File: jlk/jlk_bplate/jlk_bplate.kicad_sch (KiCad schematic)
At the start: 16 parts

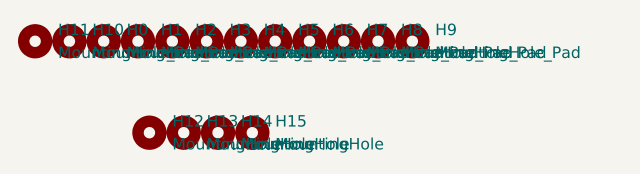
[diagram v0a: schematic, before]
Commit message: Switched to SMD diode, col2row.
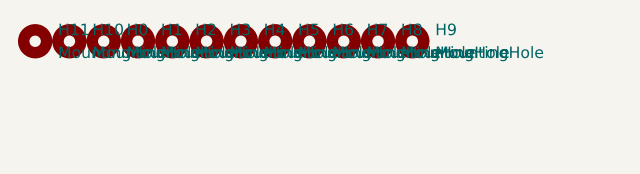
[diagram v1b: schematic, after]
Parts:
- removed H12, H13, H14, H15: MountingHole, MountingHole:MountingHole_2.2mm_M2_ISO7380_Pad, symbol Mechanical:MountingHole
- H0, H1, H10, H11, H2, H3, H4, H5, H6, H7, H8, H9: value MountingHole_Pad -> MountingHole
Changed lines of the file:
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@@
       (effects (font (size 1.27 1.27)) (justify left))
     )
-    (property "Value" "MountingHole_Pad" (at 363.22 34.29 0)
+    (property "Value" "MountingHole" (at 363.22 34.29 0)
       (effects (font (size 1.27 1.27)) (justify left))
     )
@@
       (effects (font (size 1.27 1.27)) (justify left))
     )
-    (property "Value" "MountingHole_Pad" (at 389.89 34.29 0)
+    (property "Value" "MountingHole" (at 389.89 34.29 0)
       (effects (font (size 1.27 1.27)) (justify left))
     )
@@
     )
   )
-  (symbol (lib_id "Mechanical:MountingHole") (at 373.38 43.18 0) (unit 1)
-    (in_bom yes) (on_board yes) (dnp no) (fields_autoplaced)
-    (property "Reference" "H15" (at 375.92 41.91 0)
-      (effects (font (size 1.27 1.27)) (justify left))
-    )
-    (property "Value" "MountingHole" (at 375.92 44.45 0)
-      (effects (font (size 1.27 1.27)) (justify left))
-    )
-    (property "Footprint" "MountingHole:MountingHole_2.2mm_M2_ISO7380_Pad" (at 373.38 43.18 0)
-      (effects (font (size 1.27 1.27)) hide)
-    )
-    (property "Datasheet" "~" (at 373.38 43.18 0)
-      (effects (font (size 1.27 1.27)) hide)
-    )
-    (instances
-      (project "jlk_bplate"
-        (path "/97127b28-60f4-45ff-835e-dccfbc833331"
-          (reference "H15") (unit 1)
-        )
-      )
-    )
-  )
   (symbol (lib_id "Mechanical:MountingHole") (at 391.16 33.02 0) (unit 1)
     (in_bom yes) (on_board yes) (dnp no) (fields_autoplaced)
@@
       (effects (font (size 1.27 1.27)) (justify left))
     )
-    (property "Value" "MountingHole_Pad" (at 393.7 34.29 0)
+    (property "Value" "MountingHole" (at 393.7 34.29 0)
       (effects (font (size 1.27 1.27)) (justify left))
     )
@@
       (effects (font (size 1.27 1.27)) (justify left))
     )
-    (property "Value" "MountingHole_Pad" (at 382.27 34.29 0)
+    (property "Value" "MountingHole" (at 382.27 34.29 0)
       (effects (font (size 1.27 1.27)) (justify left))
     )
@@
       (effects (font (size 1.27 1.27)) (justify left))
     )
-    (property "Value" "MountingHole_Pad" (at 367.03 34.29 0)
+    (property "Value" "MountingHole" (at 367.03 34.29 0)
       (effects (font (size 1.27 1.27)) (justify left))
     )
@@
       (effects (font (size 1.27 1.27)) (justify left))
     )
-    (property "Value" "MountingHole_Pad" (at 374.65 34.29 0)
+    (property "Value" "MountingHole" (at 374.65 34.29 0)
       (effects (font (size 1.27 1.27)) (justify left))
     )
@@
     )
   )
-  (symbol (lib_id "Mechanical:MountingHole") (at 369.57 43.18 0) (unit 1)
-    (in_bom yes) (on_board yes) (dnp no) (fields_autoplaced)
-    (property "Reference" "H14" (at 372.11 41.91 0)
-      (effects (font (size 1.27 1.27)) (justify left))
-    )
-    (property "Value" "MountingHole" (at 372.11 44.45 0)
-      (effects (font (size 1.27 1.27)) (justify left))
-    )
-    (property "Footprint" "MountingHole:MountingHole_2.2mm_M2_ISO7380_Pad" (at 369.57 43.18 0)
-      (effects (font (size 1.27 1.27)) hide)
-    )
-    (property "Datasheet" "~" (at 369.57 43.18 0)
-      (effects (font (size 1.27 1.27)) hide)
-    )
-    (instances
-      (project "jlk_bplate"
-        (path "/97127b28-60f4-45ff-835e-dccfbc833331"
-          (reference "H14") (unit 1)
-        )
-      )
-    )
-  )
   (symbol (lib_id "Mechanical:MountingHole") (at 368.3 33.02 0) (unit 1)
     (in_bom yes) (on_board yes) (dnp no) (fields_autoplaced)
@@
       (effects (font (size 1.27 1.27)) (justify left))
     )
-    (property "Value" "MountingHole_Pad" (at 370.84 34.29 0)
+    (property "Value" "MountingHole" (at 370.84 34.29 0)
       (effects (font (size 1.27 1.27)) (justify left))
     )
@@
     )
   )
-  (symbol (lib_id "Mechanical:MountingHole") (at 361.95 43.18 0) (unit 1)
-    (in_bom yes) (on_board yes) (dnp no) (fields_autoplaced)
-    (property "Reference" "H12" (at 364.49 41.91 0)
-      (effects (font (size 1.27 1.27)) (justify left))
-    )
-    (property "Value" "MountingHole" (at 364.49 44.45 0)
-      (effects (font (size 1.27 1.27)) (justify left))
-    )
-    (property "Footprint" "MountingHole:MountingHole_2.2mm_M2_ISO7380_Pad" (at 361.95 43.18 0)
-      (effects (font (size 1.27 1.27)) hide)
-    )
-    (property "Datasheet" "~" (at 361.95 43.18 0)
-      (effects (font (size 1.27 1.27)) hide)
-    )
-    (instances
-      (project "jlk_bplate"
-        (path "/97127b28-60f4-45ff-835e-dccfbc833331"
-          (reference "H12") (unit 1)
-        )
-      )
-    )
-  )
   (symbol (lib_id "Mechanical:MountingHole") (at 375.92 33.02 0) (unit 1)
     (in_bom yes) (on_board yes) (dnp no) (fields_autoplaced)
@@
       (effects (font (size 1.27 1.27)) (justify left))
     )
-    (property "Value" "MountingHole_Pad" (at 378.46 34.29 0)
+    (property "Value" "MountingHole" (at 378.46 34.29 0)
       (effects (font (size 1.27 1.27)) (justify left))
     )
@@
       (effects (font (size 1.27 1.27)) (justify left))
     )
-    (property "Value" "MountingHole_Pad" (at 351.79 34.29 0)
+    (property "Value" "MountingHole" (at 351.79 34.29 0)
       (effects (font (size 1.27 1.27)) (justify left))
     )
@@
       (effects (font (size 1.27 1.27)) (justify left))
     )
-    (property "Value" "MountingHole_Pad" (at 386.08 34.29 0)
+    (property "Value" "MountingHole" (at 386.08 34.29 0)
       (effects (font (size 1.27 1.27)) (justify left))
     )
@@
       (effects (font (size 1.27 1.27)) (justify left))
     )
-    (property "Value" "MountingHole_Pad" (at 355.6 34.29 0)
+    (property "Value" "MountingHole" (at 355.6 34.29 0)
       (effects (font (size 1.27 1.27)) (justify left))
     )
@@
       (effects (font (size 1.27 1.27)) (justify left))
     )
-    (property "Value" "MountingHole_Pad" (at 359.41 34.29 0)
+    (property "Value" "MountingHole" (at 359.41 34.29 0)
       (effects (font (size 1.27 1.27)) (justify left))
     )
@@
         )
       )
-    )
-  )
-  (symbol (lib_id "Mechanical:MountingHole") (at 365.76 43.18 0) (unit 1)
-    (in_bom yes) (on_board yes) (dnp no) (fields_autoplaced)
-    (property "Reference" "H13" (at 368.3 41.91 0)
-      (effects (font (size 1.27 1.27)) (justify left))
-    )
-    (property "Value" "MountingHole" (at 368.3 44.45 0)
-      (effects (font (size 1.27 1.27)) (justify left))
-    )
-    (property "Footprint" "MountingHole:MountingHole_2.2mm_M2_ISO7380_Pad" (at 365.76 43.18 0)
-      (effects (font (size 1.27 1.27)) hide)
-    )
-    (property "Datasheet" "~" (at 365.76 43.18 0)
-      (effects (font (size 1.27 1.27)) hide)
-    )
-    (instances
-      (project "jlk_bplate"
-        (path "/97127b28-60f4-45ff-835e-dccfbc833331"
-          (reference "H13") (unit 1)
-        )
-      )

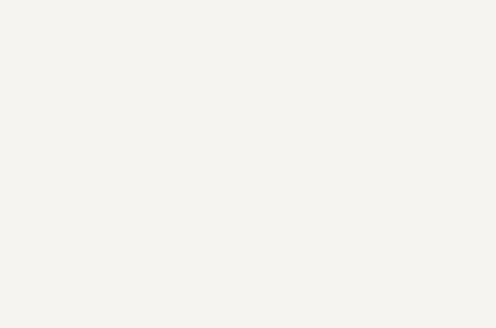
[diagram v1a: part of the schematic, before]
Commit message: Changed the reset button on the jlk.
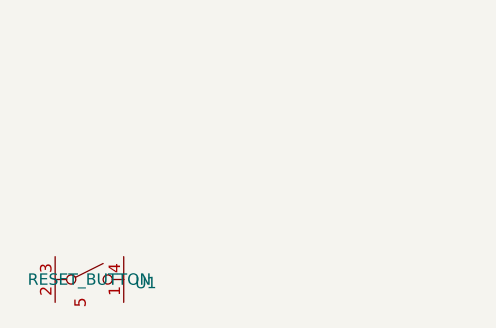
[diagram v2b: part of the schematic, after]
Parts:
- added U1: RESET_BUTTON, MountingHole:MountingHole_8.4mm_M8, symbol symbols:RESET_BUTTON
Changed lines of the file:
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@@
+    )
+  )
+  (symbol (lib_id "symbols:RESET_BUTTON") (at 212.09 152.4 270) (unit 1)
+    (in_bom yes) (on_board yes) (dnp no) (fields_autoplaced)
+    (property "Reference" "U1" (at 217.17 152.781 90)
+      (effects (font (size 1.27 1.27)) (justify left))
+    )
+    (property "Value" "RESET_BUTTON" (at 212.09 152.4 90)
+      (effects (font (size 1.27 1.27)))
+    )
+    (property "Footprint" "MountingHole:MountingHole_8.4mm_M8" (at 212.09 152.4 90)
+      (effects (font (size 1.27 1.27)) hide)
+    )
+    (property "Datasheet" "" (at 212.09 152.4 90)
+      (effects (font (size 1.27 1.27)) hide)
+    )
+    (pin "2")
+    (pin "3")
+    (pin "4")
+    (pin "5")
+    (pin "1")
+    (instances
+      (project "jlk_bplate"
+        (path "/97127b28-60f4-45ff-835e-dccfbc833331"
+          (reference "U1") (unit 1)
+        )
+      )
     )
   )

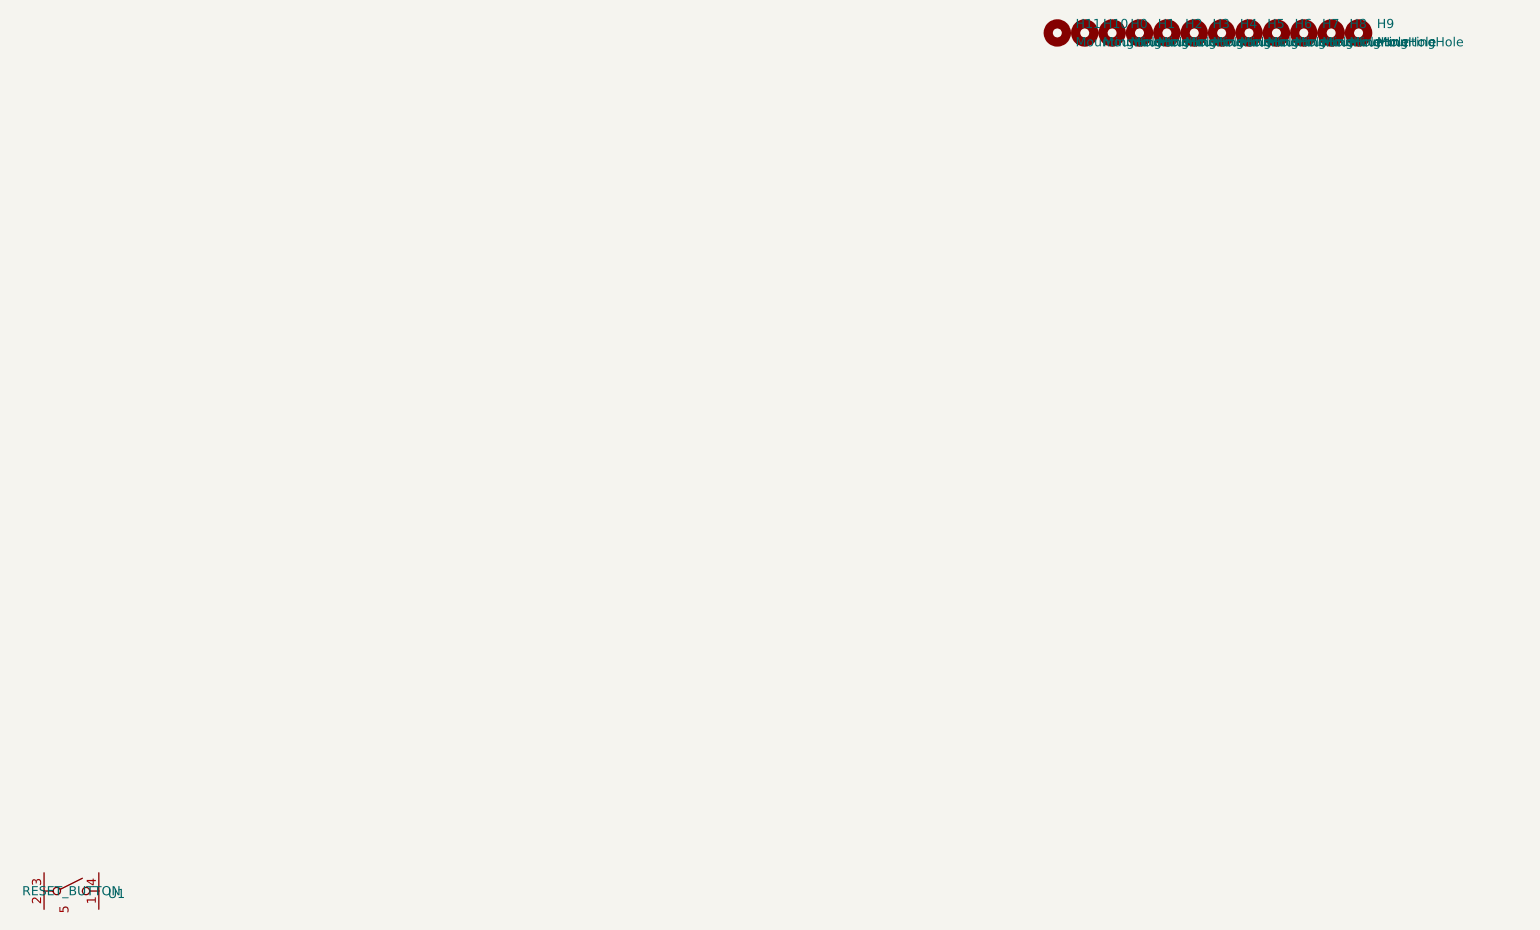
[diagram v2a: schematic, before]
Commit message: Changed jlk for mounting promicro under the pcb.
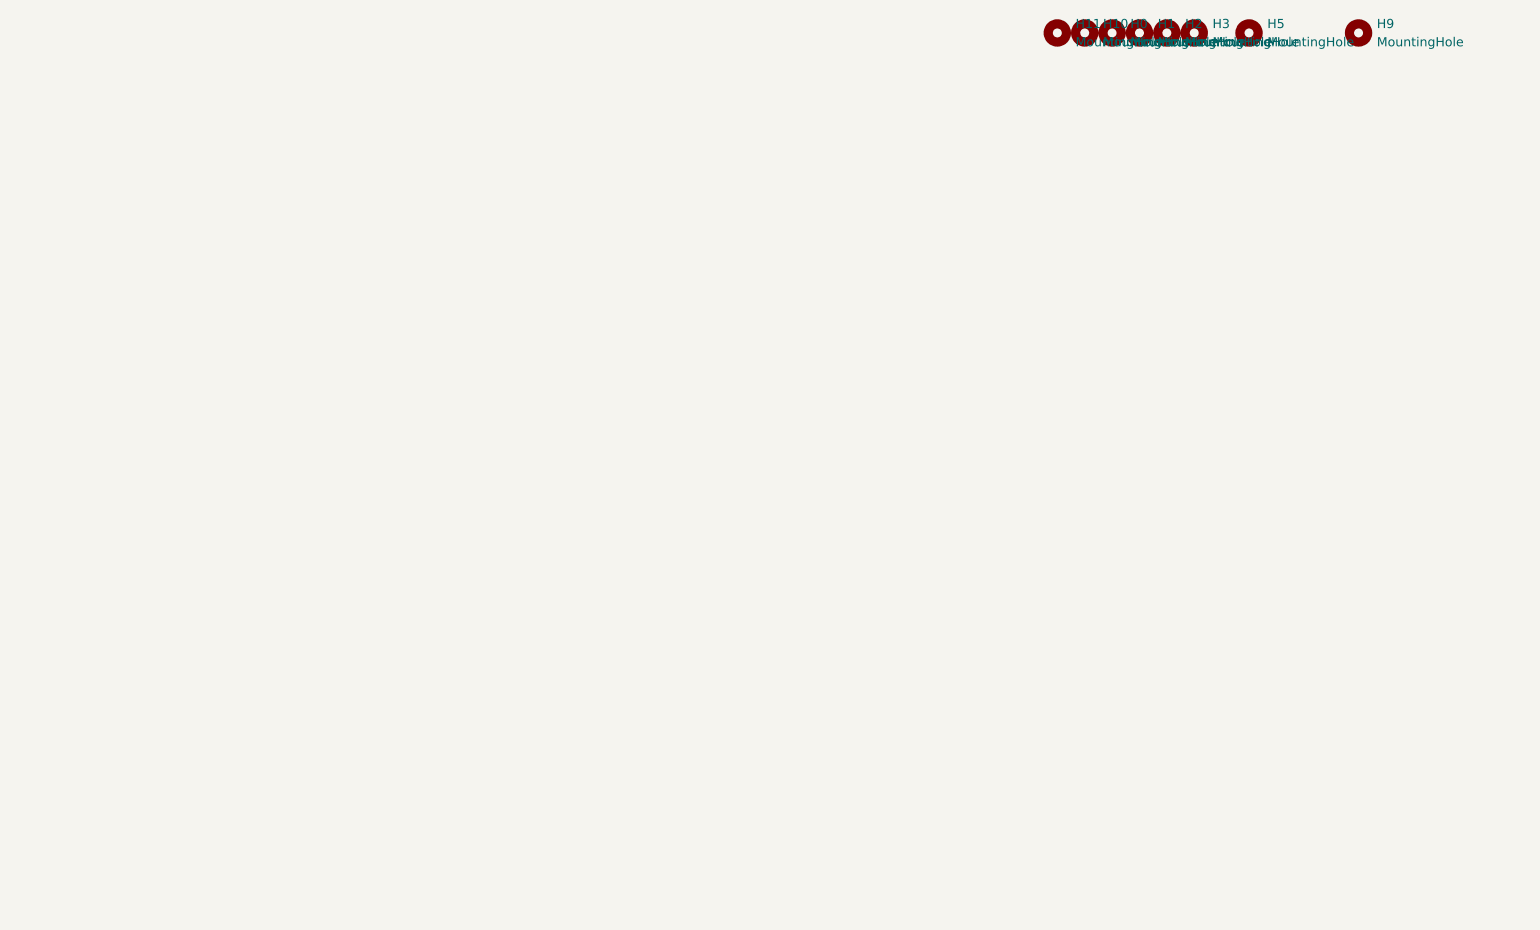
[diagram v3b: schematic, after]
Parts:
- removed H4, H6, H7, H8: MountingHole, MountingHole:MountingHole_2.2mm_M2_ISO7380_Pad, symbol Mechanical:MountingHole
- removed U1: RESET_BUTTON, MountingHole:MountingHole_8.4mm_M8, symbol symbols:RESET_BUTTON
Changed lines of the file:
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@@
-    )
-  )
-  (symbol (lib_id "Mechanical:MountingHole") (at 387.35 33.02 0) (unit 1)
-    (in_bom yes) (on_board yes) (dnp no) (fields_autoplaced)
-    (property "Reference" "H8" (at 389.89 31.75 0)
-      (effects (font (size 1.27 1.27)) (justify left))
-    )
-    (property "Value" "MountingHole" (at 389.89 34.29 0)
-      (effects (font (size 1.27 1.27)) (justify left))
-    )
-    (property "Footprint" "MountingHole:MountingHole_2.2mm_M2_ISO7380_Pad" (at 387.35 33.02 0)
-      (effects (font (size 1.27 1.27)) hide)
-    )
-    (property "Datasheet" "~" (at 387.35 33.02 0)
-      (effects (font (size 1.27 1.27)) hide)
-    )
-    (instances
-      (project "jlk_bplate"
-        (path "/97127b28-60f4-45ff-835e-dccfbc833331"
-          (reference "H8") (unit 1)
-        )
-      )
     )
   )
@@
     )
   )
-  (symbol (lib_id "symbols:RESET_BUTTON") (at 212.09 152.4 270) (unit 1)
-    (in_bom yes) (on_board yes) (dnp no) (fields_autoplaced)
-    (property "Reference" "U1" (at 217.17 152.781 90)
-      (effects (font (size 1.27 1.27)) (justify left))
-    )
-    (property "Value" "RESET_BUTTON" (at 212.09 152.4 90)
-      (effects (font (size 1.27 1.27)))
-    )
-    (property "Footprint" "MountingHole:MountingHole_8.4mm_M8" (at 212.09 152.4 90)
-      (effects (font (size 1.27 1.27)) hide)
-    )
-    (property "Datasheet" "" (at 212.09 152.4 90)
-      (effects (font (size 1.27 1.27)) hide)
-    )
-    (pin "2")
-    (pin "3")
-    (pin "4")
-    (pin "5")
-    (pin "1")
-    (instances
-      (project "jlk_bplate"
-        (path "/97127b28-60f4-45ff-835e-dccfbc833331"
-          (reference "U1") (unit 1)
-        )
-      )
-    )
-  )
-  (symbol (lib_id "Mechanical:MountingHole") (at 379.73 33.02 0) (unit 1)
-    (in_bom yes) (on_board yes) (dnp no) (fields_autoplaced)
-    (property "Reference" "H6" (at 382.27 31.75 0)
-      (effects (font (size 1.27 1.27)) (justify left))
-    )
-    (property "Value" "MountingHole" (at 382.27 34.29 0)
-      (effects (font (size 1.27 1.27)) (justify left))
-    )
-    (property "Footprint" "MountingHole:MountingHole_2.2mm_M2_ISO7380_Pad" (at 379.73 33.02 0)
-      (effects (font (size 1.27 1.27)) hide)
-    )
-    (property "Datasheet" "~" (at 379.73 33.02 0)
-      (effects (font (size 1.27 1.27)) hide)
-    )
-    (instances
-      (project "jlk_bplate"
-        (path "/97127b28-60f4-45ff-835e-dccfbc833331"
-          (reference "H6") (unit 1)
-        )
-      )
-    )
-  )
   (symbol (lib_id "Mechanical:MountingHole") (at 364.49 33.02 0) (unit 1)
     (in_bom yes) (on_board yes) (dnp no) (fields_autoplaced)
@@
         (path "/97127b28-60f4-45ff-835e-dccfbc833331"
           (reference "H2") (unit 1)
-        )
-      )
-    )
-  )
-  (symbol (lib_id "Mechanical:MountingHole") (at 372.11 33.02 0) (unit 1)
-    (in_bom yes) (on_board yes) (dnp no) (fields_autoplaced)
-    (property "Reference" "H4" (at 374.65 31.75 0)
-      (effects (font (size 1.27 1.27)) (justify left))
-    )
-    (property "Value" "MountingHole" (at 374.65 34.29 0)
-      (effects (font (size 1.27 1.27)) (justify left))
-    )
-    (property "Footprint" "MountingHole:MountingHole_2.2mm_M2_ISO7380_Pad" (at 372.11 33.02 0)
-      (effects (font (size 1.27 1.27)) hide)
-    )
-    (property "Datasheet" "~" (at 372.11 33.02 0)
-      (effects (font (size 1.27 1.27)) hide)
-    )
-    (instances
-      (project "jlk_bplate"
-        (path "/97127b28-60f4-45ff-835e-dccfbc833331"
-          (reference "H4") (unit 1)
         )
       )
@@
         )
       )
-    )
-  )
-  (symbol (lib_id "Mechanical:MountingHole") (at 383.54 33.02 0) (unit 1)
-    (in_bom yes) (on_board yes) (dnp no) (fields_autoplaced)
-    (property "Reference" "H7" (at 386.08 31.75 0)
-      (effects (font (size 1.27 1.27)) (justify left))
-    )
-    (property "Value" "MountingHole" (at 386.08 34.29 0)
-      (effects (font (size 1.27 1.27)) (justify left))
-    )
-    (property "Footprint" "MountingHole:MountingHole_2.2mm_M2_ISO7380_Pad" (at 383.54 33.02 0)
-      (effects (font (size 1.27 1.27)) hide)
-    )
-    (property "Datasheet" "~" (at 383.54 33.02 0)
-      (effects (font (size 1.27 1.27)) hide)
-    )
-    (instances
-      (project "jlk_bplate"
-        (path "/97127b28-60f4-45ff-835e-dccfbc833331"
-          (reference "H7") (unit 1)
-        )
-      )
